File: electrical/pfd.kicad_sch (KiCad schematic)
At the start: 9 parts

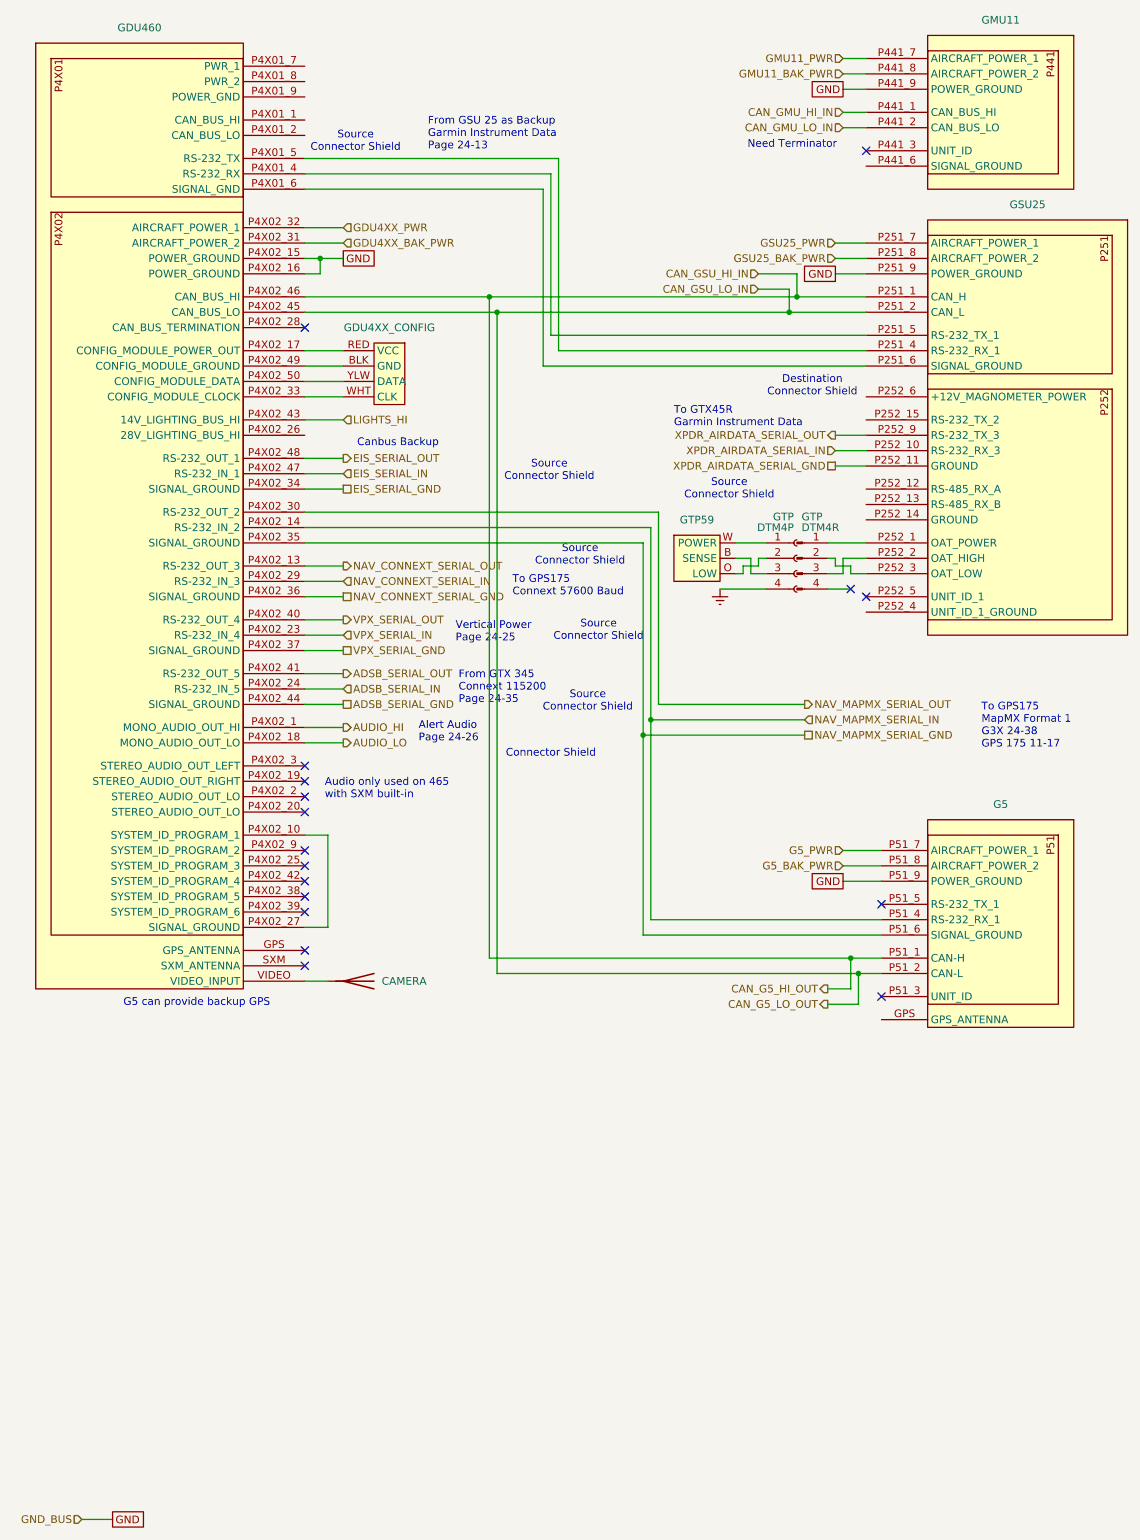
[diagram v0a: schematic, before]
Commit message: Interim check-in getting colors correct.
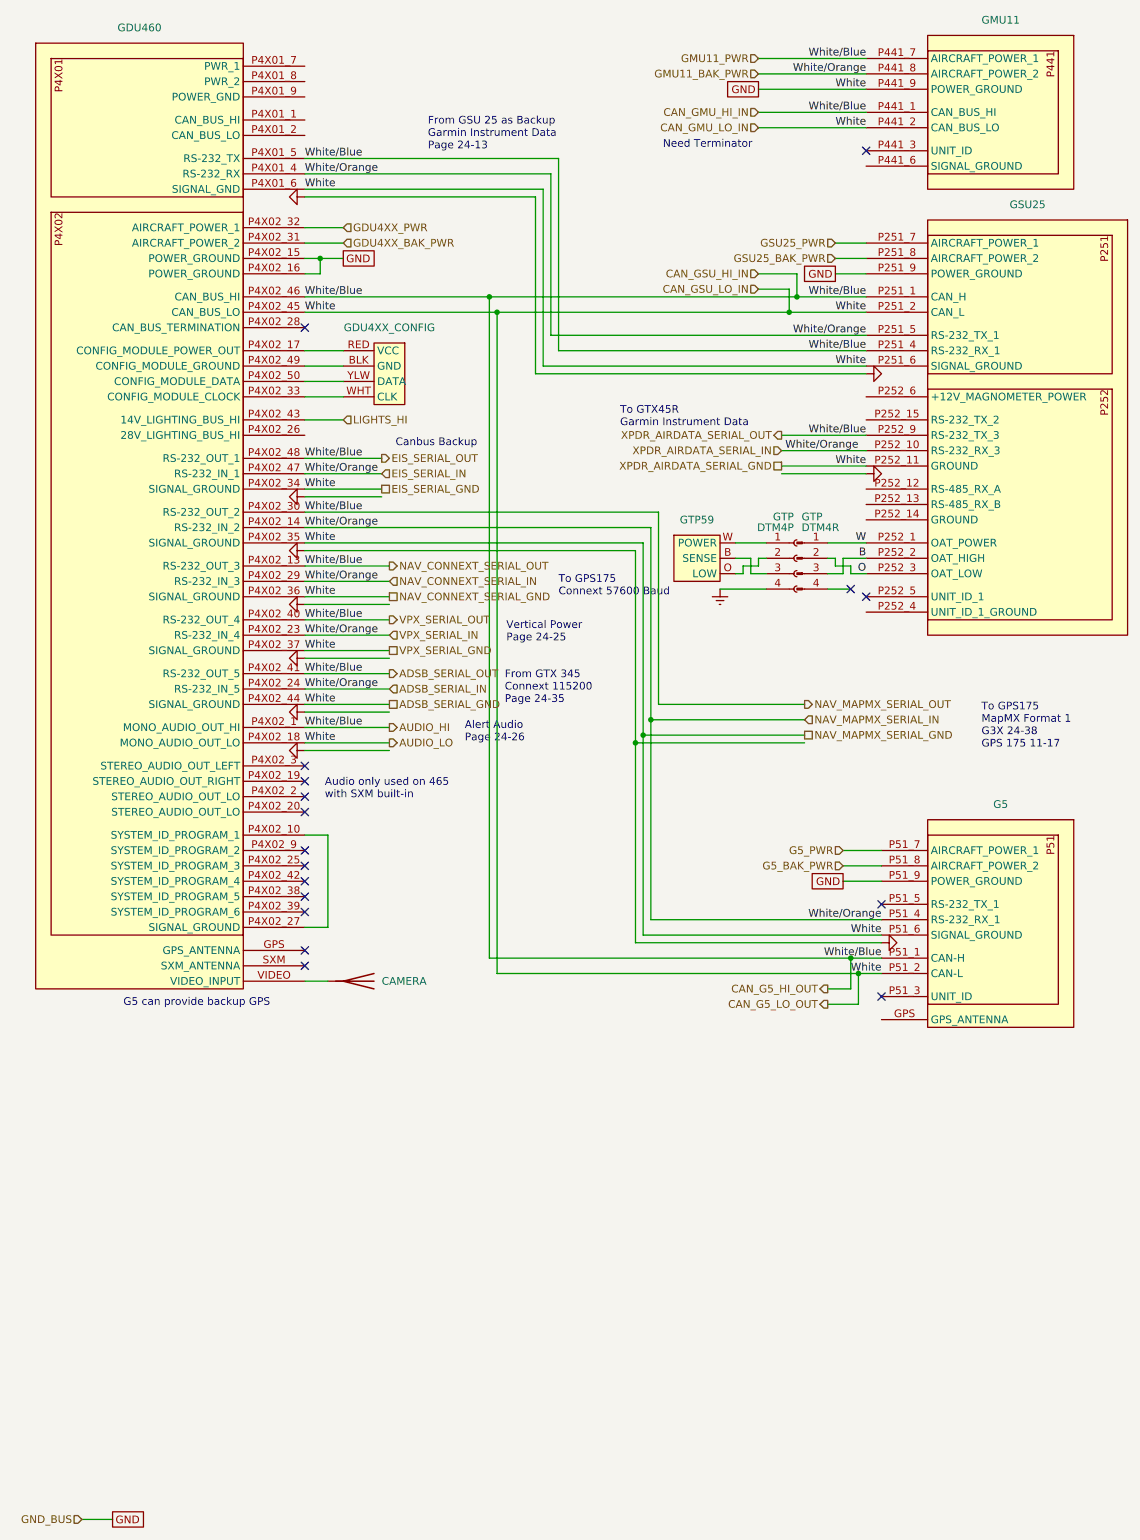
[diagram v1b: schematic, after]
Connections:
- net ADSB_SERIAL_GND is gone; now on net GND: GDU460.P4X02_44 (SIGNAL_GROUND)
- net AUDIO_HI is gone; now on net ADSB_SERIAL_OUT: GDU460.P4X02_1 (MONO_AUDIO_OUT_HI)
- net AUDIO_LO is gone; now on net GND: GDU460.P4X02_18 (MONO_AUDIO_OUT_LO)
- net CAN_G5_HI_OUT is gone; now on net ADSB_SERIAL_OUT: G5.P51_1 (CAN-H), GDU460.P4X02_46 (CAN_BUS_HI), GSU25.P251_1 (CAN_H)
- net CAN_G5_LO_OUT is gone; now on net GND: G5.P51_2 (CAN-L), GDU460.P4X02_45 (CAN_BUS_LO), GSU25.P251_2 (CAN_L)
- net CAN_GMU_HI_IN is gone; now on net ADSB_SERIAL_OUT: GMU11.P441_1 (CAN_BUS_HI)
- net CAN_GMU_LO_IN is gone; now on net GND: GMU11.P441_2 (CAN_BUS_LO)
- net EIS_SERIAL_GND is gone; now on net GND: GDU460.P4X02_34 (SIGNAL_GROUND)
- net EIS_SERIAL_IN is gone; now on net ADSB_SERIAL_IN: GDU460.P4X02_47 (RS-232_IN_1)
- net EIS_SERIAL_OUT is gone; now on net ADSB_SERIAL_OUT: GDU460.P4X02_48 (RS-232_OUT_1)
- net GMU11_BAK_PWR is gone; now on net ADSB_SERIAL_IN: GMU11.P441_8 (AIRCRAFT_POWER_2)
- net GMU11_PWR is gone; now on net ADSB_SERIAL_OUT: GMU11.P441_7 (AIRCRAFT_POWER_1)
- net NAV_CONNEXT_SERIAL_GND is gone; now on net GND: GDU460.P4X02_36 (SIGNAL_GROUND)
- net NAV_CONNEXT_SERIAL_IN is gone; now on net ADSB_SERIAL_IN: GDU460.P4X02_29 (RS-232_IN_3)
- net NAV_CONNEXT_SERIAL_OUT is gone; now on net ADSB_SERIAL_OUT: GDU460.P4X02_13 (RS-232_OUT_3)
- net NAV_MAPMX_SERIAL_GND is gone; now on net GND: G5.P51_6 (SIGNAL_GROUND), GDU460.P4X02_35 (SIGNAL_GROUND)
- net NAV_MAPMX_SERIAL_IN is gone; now on net ADSB_SERIAL_IN: G5.P51_4 (RS-232_RX_1), GDU460.P4X02_14 (RS-232_IN_2)
- net NAV_MAPMX_SERIAL_OUT is gone; now on net ADSB_SERIAL_OUT: GDU460.P4X02_30 (RS-232_OUT_2)
- net VPX_SERIAL_GND is gone; now on net GND: GDU460.P4X02_37 (SIGNAL_GROUND)
- net VPX_SERIAL_IN is gone; now on net ADSB_SERIAL_IN: GDU460.P4X02_23 (RS-232_IN_4)
- net VPX_SERIAL_OUT is gone; now on net ADSB_SERIAL_OUT: GDU460.P4X02_40 (RS-232_OUT_4)
- net XPDR_AIRDATA_SERIAL_GND is gone; now on net GND: GSU25.P252_11 (GROUND)
- net XPDR_AIRDATA_SERIAL_IN is gone; now on net ADSB_SERIAL_IN: GSU25.P252_10 (RS-232_RX_3)
- net XPDR_AIRDATA_SERIAL_OUT is gone; now on net ADSB_SERIAL_OUT: GSU25.P252_9 (RS-232_TX_3)
- net ADSB_SERIAL_IN: now also GDU460.P4X01_4 (RS-232_RX), GSU25.P251_5 (RS-232_TX_1)
- net ADSB_SERIAL_OUT: now also GDU460.P4X01_5 (RS-232_TX), GSU25.P251_4 (RS-232_RX_1)
- net GND: now also GDU460.P4X01_6 (SIGNAL_GND), GSU25.P251_6 (SIGNAL_GROUND)
- net W: now reaches GSU25.P252_1 (OAT_POWER), GTP.1 (Pin_1)
- net O: now reaches GSU25.P252_3 (OAT_LOW), GTP.2 (Pin_2)
- net B: now reaches GSU25.P252_2 (OAT_HIGH), GTP.3 (Pin_3)
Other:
- note removed: "Connector Shield"
- note removed: "Destination Connector Shield"
- note removed: "Source Connector Shield"

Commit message: Added shielding and wire colors and corrections.
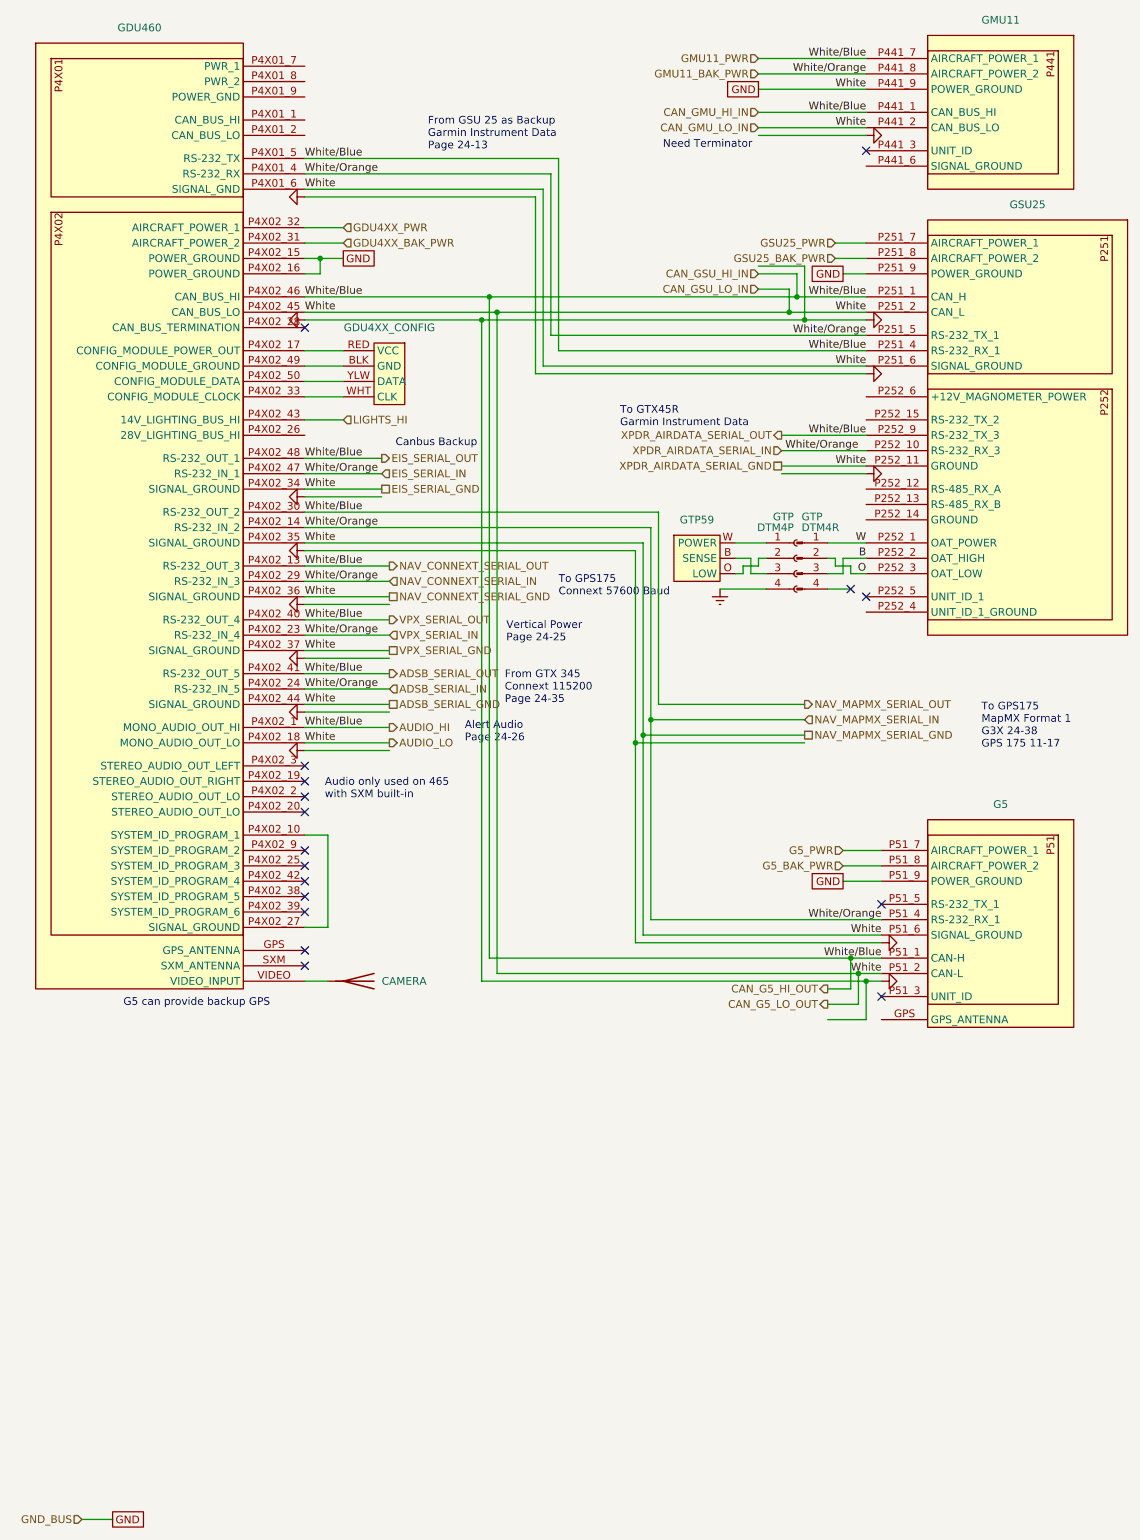
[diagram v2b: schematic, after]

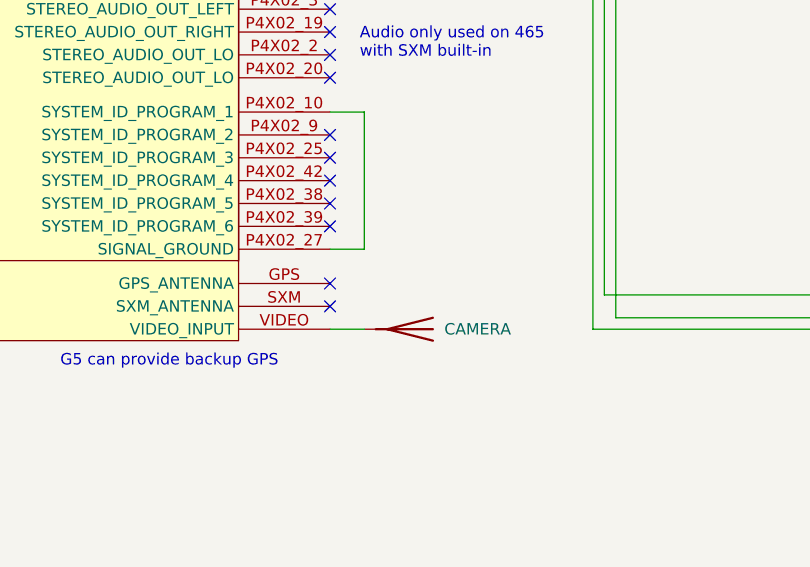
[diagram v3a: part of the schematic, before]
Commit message: Removed ground wire to surefly left ignition. Added GPS antenna to GDU.
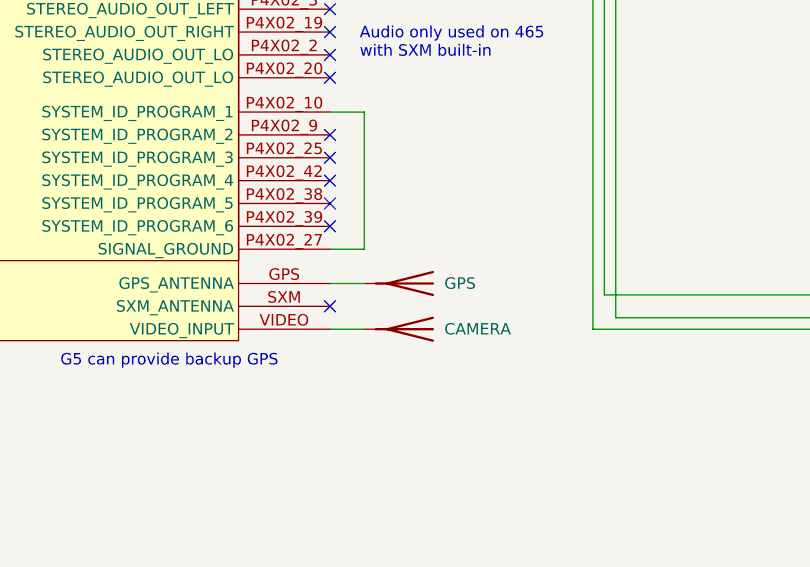
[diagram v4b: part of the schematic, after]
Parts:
- added GPS: Antenna, symbol Device:Antenna
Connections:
- net at GDU460.GPS (GPS_ANTENNA): now also GPS.1 (A)
- no-connect marks 17 -> 16
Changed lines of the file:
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@@
 		(at 62.23 137.16)
 	)
-	(no_connect
-		(at 62.23 167.64)
-	)
 	(wire
 		(pts
@@
 		(pts
 			(xy 151.13 153.67) (xy 157.48 153.67)
+		)
+		(stroke
+			(width 0)
+			(type default)
+		)
+	)
+	(wire
+		(pts
+			(xy 62.23 167.64) (xy 66.04 167.64)
 		)
 		(stroke
@@
 					(unit 1)
 				)
+			)
+		)
+	)
+	(symbol
+		(lib_id "Device:Antenna")
+		(at 71.12 167.64 270)
+		(unit 1)
+		(exclude_from_sim no)
+		(in_bom yes)
+		(on_board yes)
+		(dnp no)
+		(fields_autoplaced yes)
+		(property "Reference" "GPS"
+			(at 74.93 167.6399 90)
+			(effects
+				(font
+					(size 1.27 1.27)
+				)
+				(justify left)
+			)
+		)
+		(property "Value" "Antenna"
+			(at 74.93 168.91 90)
+			(effects
+				(font
+					(size 1.27 1.27)
+				)
+				(justify left)
+				(hide yes)
+			)
+		)
+		(property "Footprint" ""
+			(at 71.12 167.64 0)
+			(effects
+				(font
+					(size 1.27 1.27)
+				)
+				(hide yes)
+			)
+		)
+		(property "Datasheet" "~"
+			(at 71.12 167.64 0)
+			(effects
+				(font
+					(size 1.27 1.27)
+				)
+				(hide yes)
+			)
+		)
+		(property "Description" ""
+			(at 71.12 167.64 0)
+			(effects
+				(font
+					(size 1.27 1.27)
+				)
+			)
+		)
+		(pin "1"
+		)
+		(instances
+			(project "electrical"
+				(path "/e8ec215a-dbe2-4eba-a577-e50a0a128049/633b5331-dc3f-449e-8212-24f89753723c"
+					(reference "GPS")
+					(unit 1)
+				)

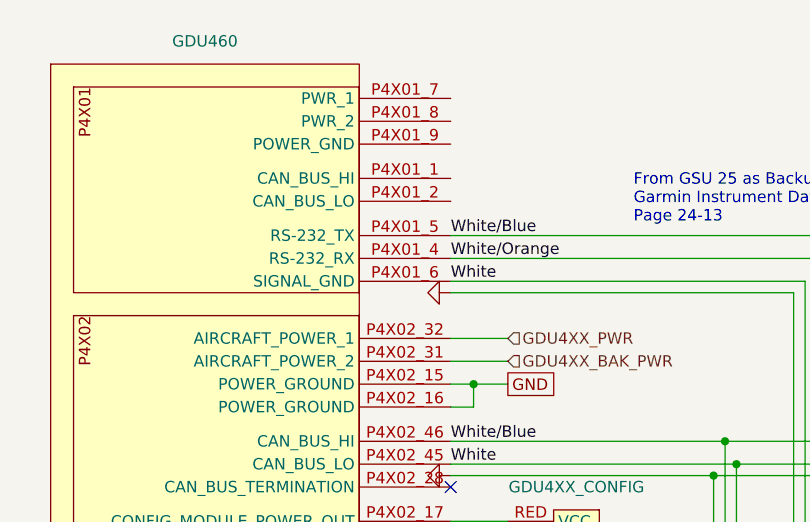
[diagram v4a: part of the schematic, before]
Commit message: Fixes GDU/GSU wiring for ADAHRS being reversed.
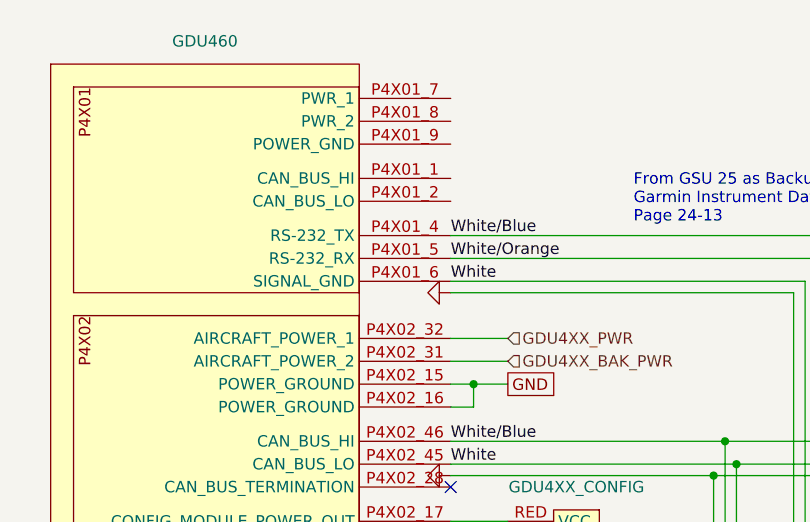
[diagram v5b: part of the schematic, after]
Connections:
- net ADSB_SERIAL_IN: now also GDU460.P4X01_5 (RS-232_RX); no longer GDU460.P4X01_4 (RS-232_RX)
- net ADSB_SERIAL_OUT: now also GDU460.P4X01_4 (RS-232_TX); no longer GDU460.P4X01_5 (RS-232_TX)
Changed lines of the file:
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@@
 	(title_block
 		(title "PFD & ADAHRS")
-		(date "2025-11-19")
-		(rev "1.2.8")
+		(date "2026-04-02")
+		(rev "1.2.12")
 		(company "N78HR")
 	)
